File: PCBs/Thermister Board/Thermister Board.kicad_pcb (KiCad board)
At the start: 2 copper layers, 18 x 20.4 mm, 20 parts, among them J1 Conn_01x03, J2 Conn_01x02, J3 Conn_01x02, J4 Conn_01x03, U1 INA826AIDRGR

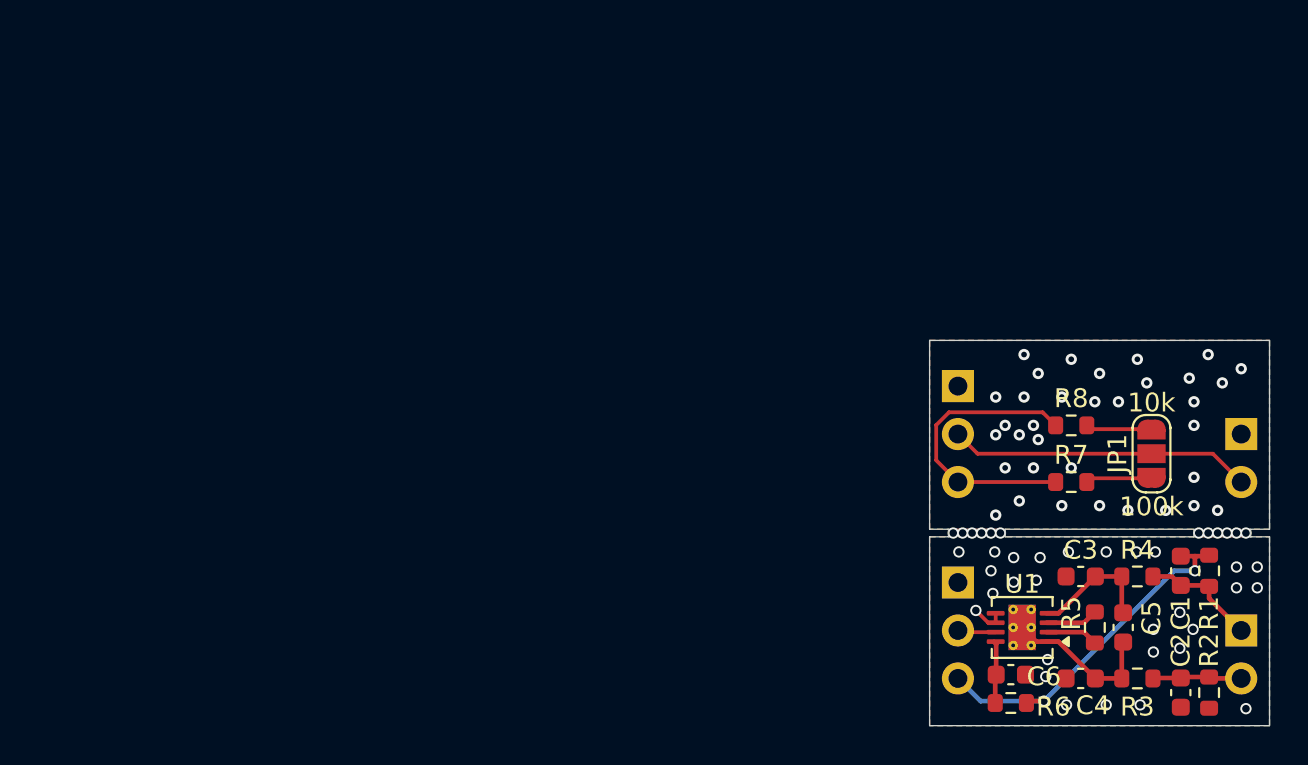
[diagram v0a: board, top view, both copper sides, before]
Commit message: Updated KiCad files and made 3D files for expansion board and thermister board
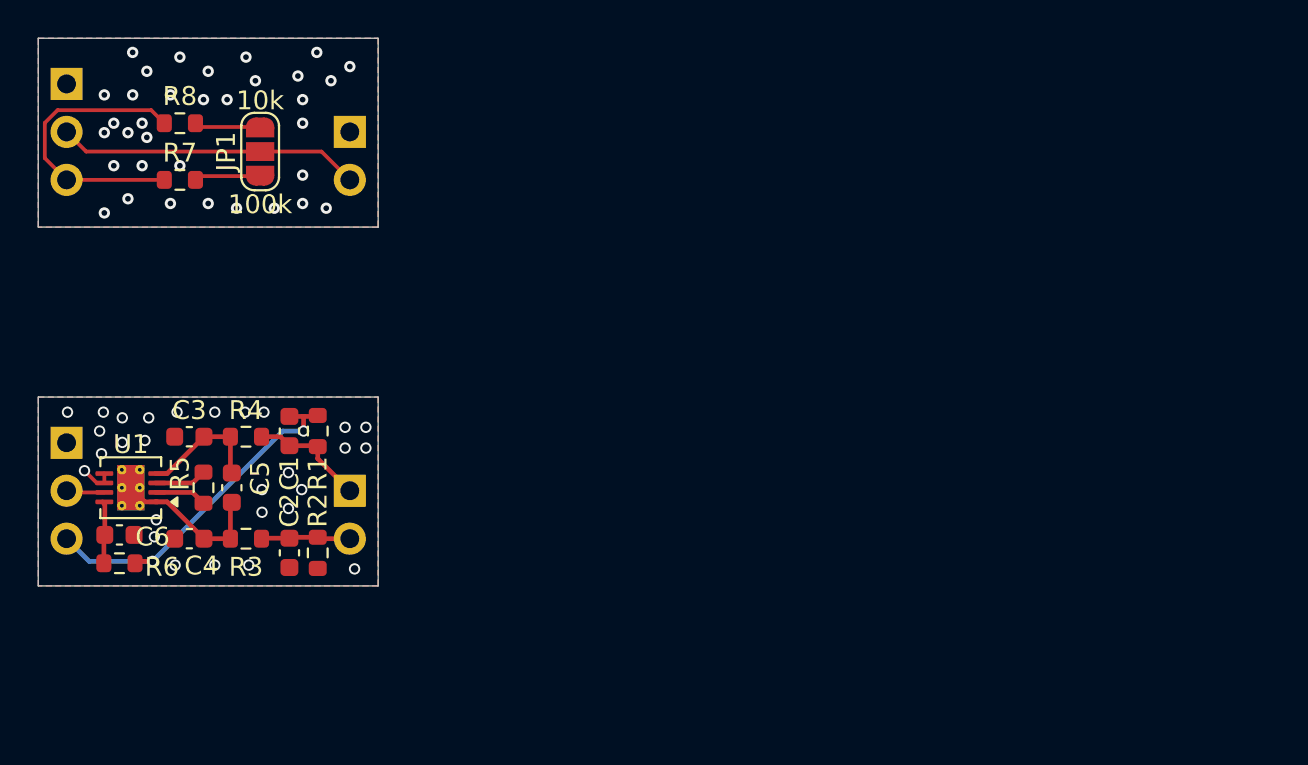
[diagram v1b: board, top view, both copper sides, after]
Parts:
- moved J3 49.8 mm to (107.5, 70.0)
- moved J4 49.8 mm to (92.5, 67.4)
- moved JP1 49.8 mm to (102.8, 71.0)
- moved R7 49.8 mm to (98.5, 72.5)
- moved R8 49.8 mm to (98.5, 69.5)
- moved C1 47.8 mm to (104.3, 85.8)
- moved C2 47.8 mm to (104.3, 92.2)
- moved C6 47.8 mm to (95.3, 91.3)
- moved R1 47.8 mm to (105.8, 85.8)
- moved R2 47.8 mm to (105.8, 92.2)
- moved R6 47.8 mm to (95.3, 92.8)
- moved C3 47.8 mm to (99.0, 86.1)
- moved C4 47.8 mm to (99.0, 91.5)
- moved C5 47.8 mm to (101.2, 88.8)
- moved J1 47.8 mm to (92.5, 86.4)
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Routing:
- net (no net): vias 12 -> 0
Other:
- board size 18 x 20.4 mm -> 18 x 29 mm
- board text added: "PCB3D_BR_NTC"
- board text added: "PCB3D_BR_PTC"
- board text added: "PCB3D_TL_NTC"
- board text added: "PCB3D_TL_PTC"
